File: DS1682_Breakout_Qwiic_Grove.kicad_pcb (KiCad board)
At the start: 2 copper layers, 20 x 24.2 mm, 15 parts, among them J1 2p-smd-1.0-90d, J2 H4P-SMD-2.0, U2 BSS138PS, U3 XC6206MR

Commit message: Add LOGO1 alternative
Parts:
- renumbered U$4 to LOGO1
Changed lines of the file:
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@@
   (module OSHW_FILLX200_NOTEXT (layer Bottom)
     (at 146.7231 113.7666 180)
-    (fp_text reference U$4 (at 0 0 180) (layer B.SilkS) hide
+    (fp_text reference LOGO1 (at 0 0 180) (layer B.SilkS) hide
       (effects (font (size 1.27 1.27) (thickness 0.15)) (justify mirror))
     )

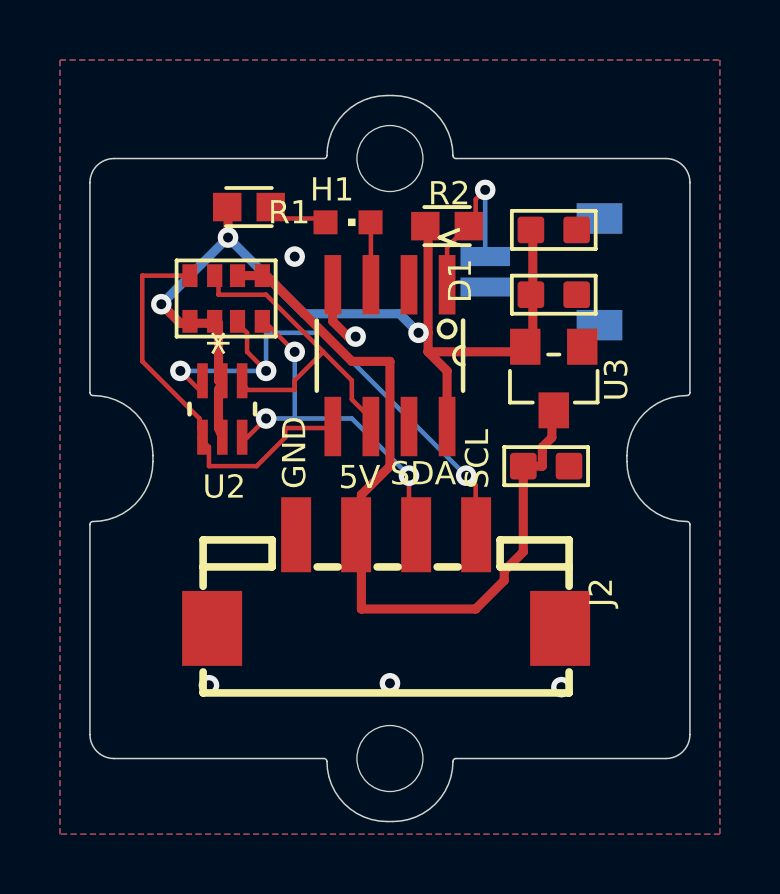
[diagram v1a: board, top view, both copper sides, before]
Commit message: Upgrade to new kicad and fix BOM parts
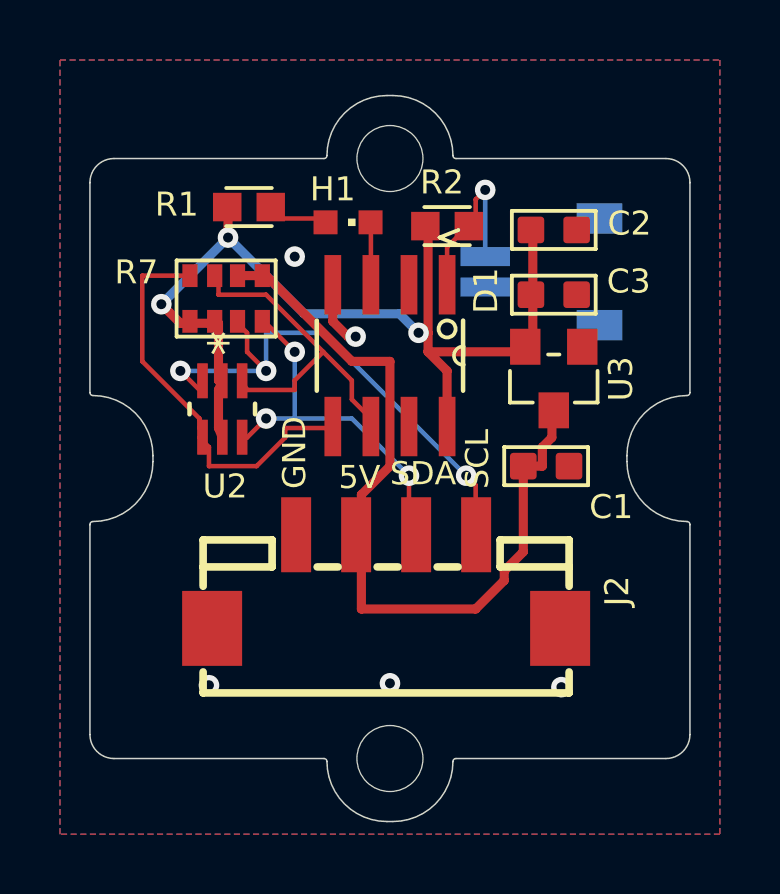
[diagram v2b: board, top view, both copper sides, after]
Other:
- net class Default removed
